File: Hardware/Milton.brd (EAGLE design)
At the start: 53 x 44.8 mm, 75 parts, among them J1 1981568-1, Q1 12MHz, U10 MAX31850K, U3 USD-SOCKETNEW, U4 MMA8452Q, U5 MIC5203-5.0YM5, U6 SI4464, U7 TPS61201, U8 BME280, U9 MMDT3904, X1 B4B-ZR

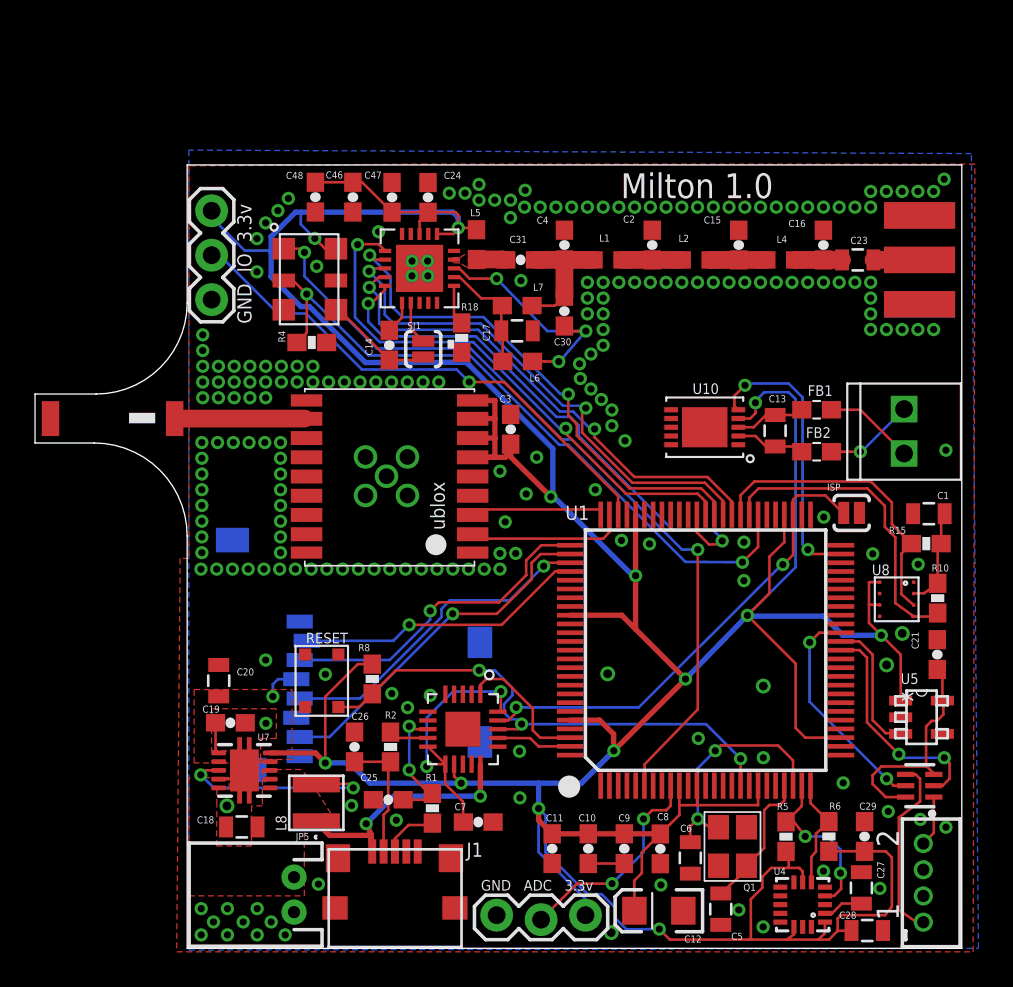
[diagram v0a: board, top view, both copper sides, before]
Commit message: Cleaning
Optimize traces, add more part numbers.
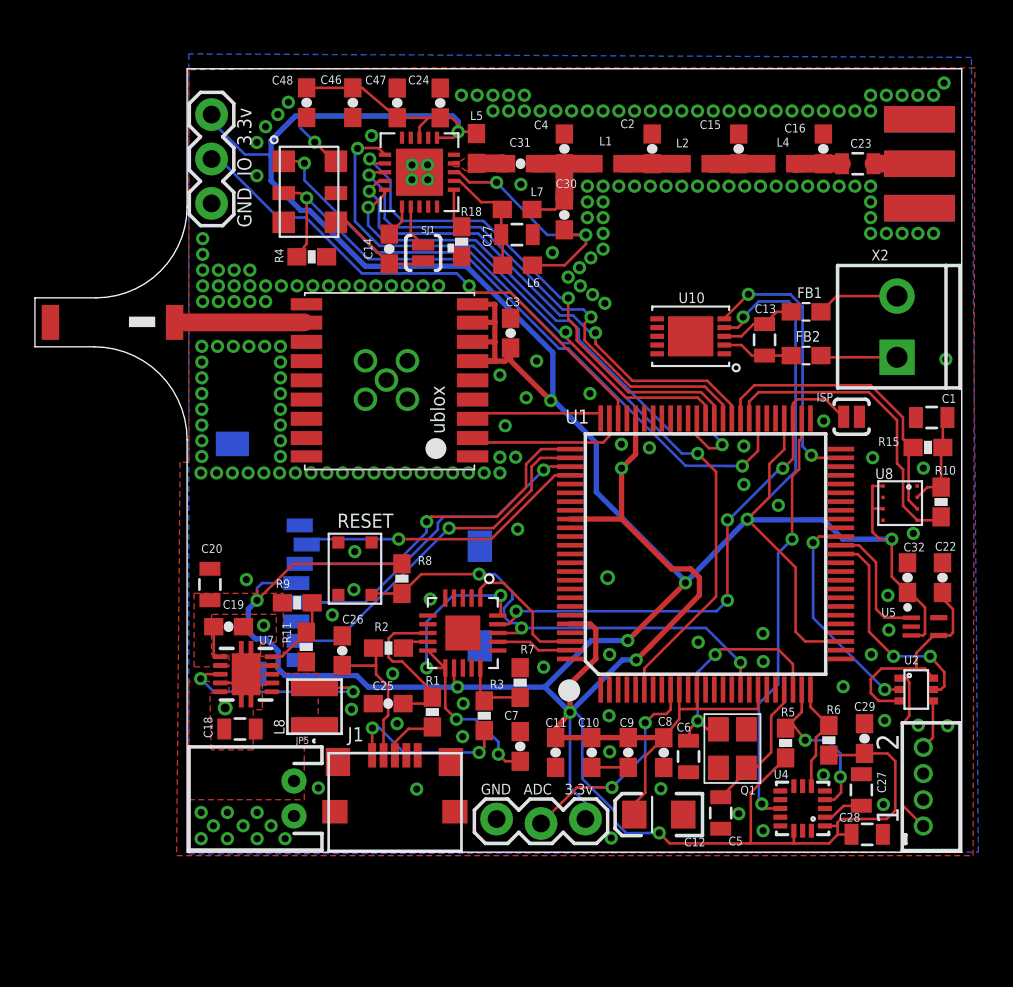
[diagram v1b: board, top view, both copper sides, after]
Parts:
- removed C21: 0.47uF, SparkFun-Capacitors:0603-CAP
- removed JP1: M022.54MM_SCREWTERM, SparkFun-Connectors:1X02_2.54_SCREWTERM
- removed U9: MMDT3904, SparkFun-DiscreteSemi:SOT363
- added C22, C32: 0.1uF, SparkFun-Capacitors:0603-CAP
- added R11: 180k, SparkFun-Resistors:0603-RES
- added R3: 4.7k, SparkFun-Resistors:0603-RES
- added R7: 10k, SparkFun-Resistors:0603-RES
- added R9: 1M, SparkFun-Resistors:0603-RES
- added U2: DDC113TU-7-F, wrea:SC70−6
- added X2: M023.5MM, SparkFun-Connectors:SCREWTERMINAL-3.5MM-2
- C7: value 100nf -> 0.1uF
- U5: value MIC5203-5.0YM5 -> TCR2EE50,LM; device wrea:SOT-23-5_M5 -> Xevelabs:SOT50P160X60-5N
- U7: value TPS61201 -> TPS61200
- moved RESET 6.68 mm to (9.60, 16.2)
- moved R8 5.98 mm to (12.3, 15.6)
- moved C6 5.80 mm to (28.7, 5.47)
- moved R2 5.66 mm to (11.5, 11.7), turned to 0 degrees
- moved FB1 5.63 mm to (35.4, 30.9)
- moved C18 5.60 mm to (3.02, 7.04)
- moved C27 5.60 mm to (38.6, 3.56)
- moved C29 5.60 mm to (38.7, 6.50)
- moved Q1 5.60 mm to (31.2, 5.92)
- moved C26 5.54 mm to (8.87, 11.5)
- moved FB2 5.53 mm to (35.4, 28.4)
- moved C20 5.52 mm to (1.30, 15.3)
- moved C9 5.50 mm to (25.2, 5.70)
- moved C10 5.50 mm to (23.1, 5.70)
- moved C11 5.50 mm to (21.1, 5.70)
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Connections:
- removed net N$16: U4.11
- new net N$1: R11.2, R9.1, U7.10
- new net N$10: J1.5, R3.2
- new net N$21: R3.1, R7.2, U$3.CBUS0
- net 3.3V: now also C32.1, R9.2, U5.3; no longer U4.7, U5.1, U7.10
- net 5V: now also C22.1, U2.3, U2.6, U5.4; no longer C21.2, U5.5, U9.3, U9.6
- net 5V_EN: now also U5.1; no longer U5.3
- net CAM1: now also U2.1; no longer U9.4
- net CAM2: now also U2.4; no longer U9.1
- net CAMERA1_EN: now also U2.2; no longer U9.5
- net CAMERA2_EN: now also U2.5; no longer U9.2
- net EINT1: now also U4.11
- net GND: now also C22.2, C32.2, R11.1, R7.1, U4.7; no longer C21.1
- net TM_RAW: now also X2.1; no longer JP1.P1
- net TP_RAW: now also X2.2; no longer JP1.P2
- net VIN: no longer J1.5, U$3.CBUS0
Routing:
- net 3.3V: track 275.4 -> 308.2 mm
- net EINT1: track 0.00 -> 24.3 mm, vias 0 -> 2
- net VIN: track 15.8 -> 0.00 mm, vias 2 -> 0
- net N$10: track 0.00 -> 9.62 mm, vias 0 -> 2
- net N$1: track 0.00 -> 4.54 mm
- net N$12: track 15.2 -> 19.5 mm, vias 2 -> 4
- net N$21: track 0.00 -> 4.15 mm
- net ISP_BOOT: track 27.6 -> 30.3 mm, vias 2 -> 4
- net RESET: track 30.5 -> 28.2 mm
- net N$4: track 7.58 -> 9.14 mm, vias 2 -> 0
- net N$9: track 7.43 -> 8.63 mm
- net CAM1: track 10.7 -> 9.53 mm
- net N$5: track 2.40 -> 1.55 mm
- net IC6_RTC2: track 14.1 -> 13.3 mm
- net TM_RAW: track 5.16 -> 4.39 mm, vias 1 -> 0
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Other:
- board text removed: "Milton 1.0"

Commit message: Update.
Shifted components to make room to break out another digital io
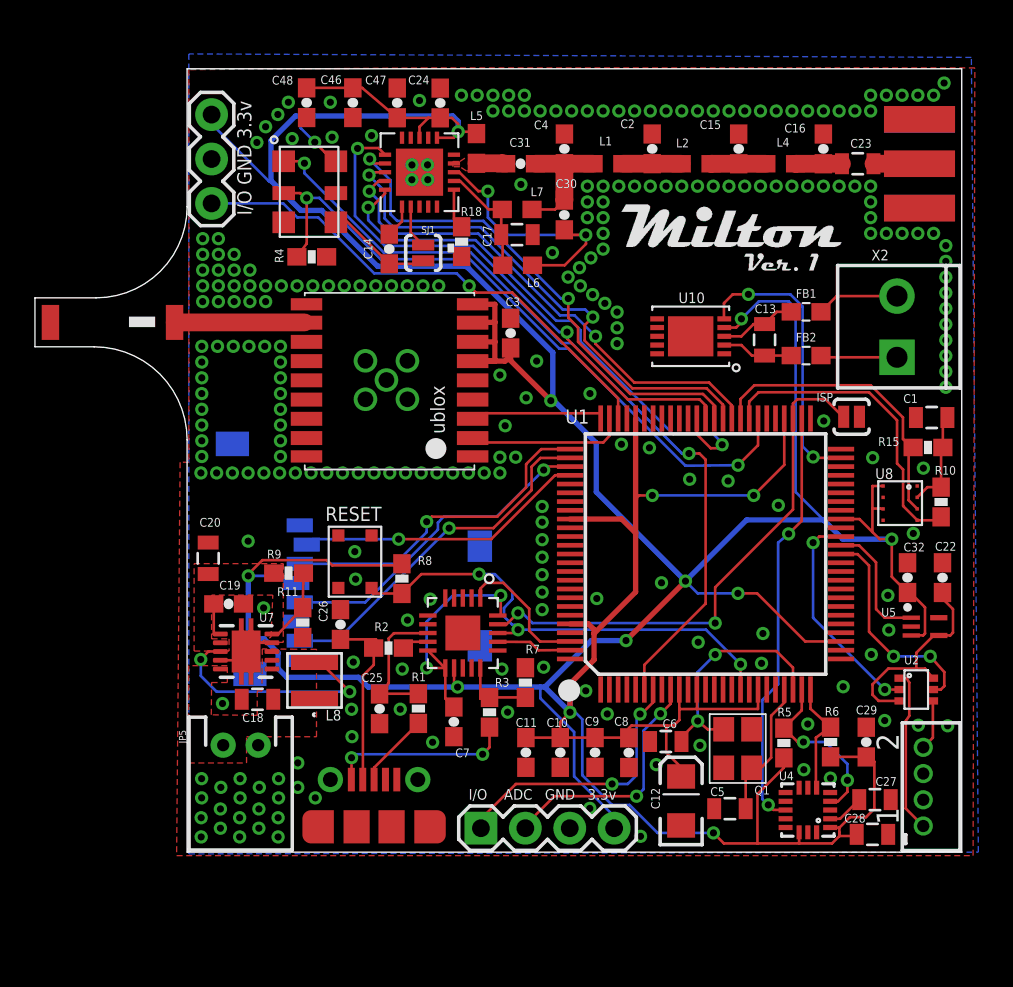
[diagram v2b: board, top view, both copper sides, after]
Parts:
- removed J1: 1981568-1, wrea:CONN_1981568-1
- removed JP2: (no value), SparkFun-Connectors:1X03_LOCK
- added JP1: (no value), SparkFun-Connectors:1X04
- added U$5: USB-CON-5PIN-105017-0001, GeekAmmo:USB-MICRO-MOLEX-105017-0001
- moved JP5 4.31 mm to (3.06, 6.12), turned to 180 degrees
- moved C7 4.05 mm to (15.3, 7.45), turned to 270 degrees
- moved C8 2.00 mm to (25.3, 5.69)
- moved C18 1.97 mm to (4.02, 8.74)
- moved C9 1.90 mm to (23.3, 5.70)
- moved C10 1.80 mm to (21.3, 5.70)
- moved R9 1.77 mm to (5.80, 16.0)
- moved C11 1.70 mm to (19.4, 5.70)
- moved C6 1.56 mm to (27.4, 6.33), turned to 180 degrees
- moved C20 1.50 mm to (1.20, 16.8)
- moved C26 1.50 mm to (8.77, 13.0)
- moved L8 1.50 mm to (7.28, 9.82)
- moved C12 1.50 mm to (28.2, 2.93), turned to 90 degrees
- moved R11 1.41 mm to (6.61, 13.1)
- moved C19 1.30 mm to (2.37, 14.2)
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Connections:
- removed net CUTDOWN: JP3.2, U1.73
- new net DIGITAL_1: JP3.1, U1.73
- new net DIGITAL_2: JP1.1, U1.7
- net 3.3V: now also JP1.4; no longer JP2.3
- net ADC_IN1: now also JP1.2; no longer JP2.2
- net GND: now also JP1.3, JP3.2, U$5.5; no longer J1.1, JP2.1, JP3.1
- net N$10: now also U$5.1; no longer J1.5
- net N$7: now also U$5.3; no longer J1.3
- net N$9: now also U$5.2; no longer J1.4
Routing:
- net CUTDOWN: track 30.2 -> 0.00 mm, vias 1 -> 0
- net DIGITAL_1: track 0.00 -> 29.0 mm, vias 0 -> 1
- net DIGITAL_2: track 0.00 -> 15.8 mm, vias 0 -> 2
- net N$12: track 19.5 -> 13.7 mm, vias 4 -> 2
- net N$9: track 8.63 -> 11.2 mm
- net ADC_IN1: track 12.3 -> 14.1 mm
- net GND: track 5.46 -> 3.95 mm, vias 216 -> 253
- net 3.3V: track 308.2 -> 306.7 mm
- net N$19: track 12.5 -> 13.9 mm
- net N$4: track 9.14 -> 7.95 mm
- net N$7: track 3.23 -> 4.26 mm
- net N$10: track 9.62 -> 10.5 mm
- net N$20: track 14.5 -> 15.3 mm
- net DAC: track 46.8 -> 46.1 mm
- net EXT_TEMP: track 15.8 -> 16.4 mm
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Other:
- board text added: "I/O ADC GND 3.3v"
- board text added: "I/O GND 3.3v"
- board text removed: "GND ADC 3.3v"
- board text removed: "GND IO 3.3v"

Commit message: Update
Continue cleaning up traces and adding part numbers
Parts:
- removed C46: 100pF, SparkFun-Capacitors:0603-CAP
- removed C47: 0.1uF, SparkFun-Capacitors:0603-CAP
- removed C48: 1uF, SparkFun-Capacitors:0603-CAP
- removed JP5: M02JST-PTH-2, SparkFun-Connectors:JST-2-PTH
- removed L8: SRN3015-2R2M, wrea:IND_BOURNS_SRN3015
- removed R15: 4.7k, SparkFun-Resistors:0603-RES
- removed U$5: USB-CON-5PIN-105017-0001, GeekAmmo:USB-MICRO-MOLEX-105017-0001
- added C21: 0.1uF, SparkFun-Capacitors:0805
- added C33: 36pF, SparkFun-Capacitors:0603-CAP
- added C34: 1000pF, SparkFun:0805
- added JP2: (no value), SparkFun-Connectors:1X03
- added L3: 220nH, SparkFun-Passives:0603
- added R12: 1k, SparkFun-Resistors:0603-RES
- added U9: BME280, wrea:BME280
- C1: value 0.1uF -> 47pF; device SparkFun-Capacitors:0805 -> SparkFun-Capacitors:0603-CAP
- C10: value 0.1uF -> 10uF; device SparkFun-Capacitors:0603-CAP -> SparkFun-Capacitors:EIA3216
- C11: device SparkFun-Capacitors:0603-CAP -> SparkFun:0603-CAP
- C12: device SparkFun-Capacitors:EIA3216 -> SparkFun-Capacitors:0805
- C13: device SparkFun-Capacitors:0805 -> SparkFun-Capacitors:0603-CAP
- C14: value 100pF -> 10uF; device SparkFun-Capacitors:0603-CAP -> SparkFun-Capacitors:0805
- C15: value 56pF -> 0.1uF
- C16: value 36pF -> 0.1uF
- C17: value 22pF -> 0.1uF; device SparkFun:0805 -> SparkFun-Capacitors:0805
- C18: value 10uF -> 4.7uF; device SparkFun-Capacitors:0805 -> SparkFun-Capacitors:0603-CAP
- C19: device SparkFun-Capacitors:0603-CAP -> SparkFun-Capacitors:0805
- C2: value 56pF -> 47pF
- C20: value 10uF -> 0.1uF
- C22: value 0.1uF -> 100pF
- C23: value 1000pF -> 1uF; device SparkFun:0805 -> SparkFun-Capacitors:0603-CAP
- C24: value 1000pF -> 0.1uF
- C25: value 47pF -> 100pF
- C26: value 47pF -> 22pF; device SparkFun-Capacitors:0603-CAP -> SparkFun:0805
- C27, C28: value 0.1uF -> 1000pF; device SparkFun-Capacitors:0805 -> SparkFun-Capacitors:0603-CAP
- C29: value 4.7uF -> 12pF
- C3: device SparkFun:0603-CAP -> SparkFun-Capacitors:0603-CAP
- C30: value 12pF -> 36pF
- C31: value 1000pF -> 56pF
- C32: value 0.1uF -> 56pF
- C4: value 36pF -> 18pF; device SparkFun-Capacitors:0603-CAP -> SparkFun-Capacitors:0805
- C6: value 18pF -> 0.1uF; device SparkFun-Capacitors:0805 -> SparkFun-Capacitors:0603-CAP
- FB1, FB2: value (none) -> FB; device LoganSmith-Inductors:0603-RES -> SparkFun-Passives:0603
- JP1: value (none) -> M02JST-PTH-2; device SparkFun-Connectors:1X04 -> SparkFun-Connectors:JST-2-PTH
- JP3: device SparkFun-Connectors:1X03 -> SparkFun-Connectors:1X04
- L1: value 68nH -> SRN3015-2R2M; device SparkFun-Passives:0603 -> wrea:IND_BOURNS_SRN3015
- L2: value 72nH -> 470nH
- L4: value 68nH -> 150nH
- L5: value 470nH -> 68nH
- L6: value 220nH -> 72nH
- L7: value 150nH -> 68nH
- R1: value 27 -> 4.7k
- R11: value 180k -> 4.7k
- R2: value 27 -> 10k
- R3: value 4.7k -> 27
- R4: value 1k -> 27
- R5: value 4.7k -> 10K
- R6: value 4.7k -> 1M
- R7: value 10k -> 180k
- R8: value 10K -> 4.7k
- R9: value 1M -> 4.7k
- U$1: value 1575AT43A40 -> USB-MICRO_105017-0001; device ava:JTI_ANTENNA-1575AT43A40 -> wrea:USB-MICRO-MOLEX-105017-0001
- U$2: value UBLOX_MAX -> 1575AT43A40; device ava:UBLOX_MAX -> ava:JTI_ANTENNA-1575AT43A40
- U$3: value FT231XQ-R -> UBLOX_MAX; device ftdi_ft231xq-r:FTDI_FT231XQ-R_PACKAGE -> ava:UBLOX_MAX
- U1: value (none) -> FT231X; device microbuilder:LQFP100 -> wrea:FT231XQ-R
- U10: value MAX31850K -> SI4464; device LoganSmith-Analog_IC:10-TDFN-EP -> ava:QFN20+GNDPAD
- U2: value DDC113TU-7-F -> (none); device wrea:SC70−6 -> microbuilder:LQFP100
- U4: value MMA8452Q -> DDC113TU-7-F; device SparkFun-Sensors:QFN-16_0.5MM -> wrea:SC70−6
- U5: value TCR2EE50,LM -> TPS61200; device Xevelabs:SOT50P160X60-5N -> texas:S-PDSO-N10
- U6: value SI4464 -> TCR2EE50,LM; device ava:QFN20+GNDPAD -> Xevelabs:SOT50P160X60-5N
- U7: value TPS61200 -> MMA8452Q; device texas:S-PDSO-N10 -> SparkFun-Sensors:QFN-16_0.5MM
- U8: value BME280 -> MAX31850K; device wrea:BME280 -> LoganSmith-Analog_IC:10-TDFN-EP
- moved C27 47.0 mm to (14.5, 42.8), turned to 270 degrees
- moved C28 43.3 mm to (19.1, 39.4), turned to 180 degrees
- moved C17 39.9 mm to (39.2, 1.02), turned to 0 degrees
- moved JP3 38.9 mm to (16.8, 1.37), turned to 0 degrees
- moved C4 38.9 mm to (31.0, 2.49), turned to 180 degrees
- moved U6 38.9 mm to (42.2, 12.9), turned to 0 degrees
- moved U5 38.9 mm to (3.37, 11.5), turned to 270 degrees
- moved C19 38.6 mm to (39.3, 3.00)
- moved R11 37.2 mm to (43.1, 20.0)
- moved C22 36.8 mm to (11.6, 34.5), turned to 270 degrees
- moved C1 35.8 mm to (8.77, 13.0), turned to 270 degrees
- moved C2 35.6 mm to (11.0, 8.20), turned to 270 degrees
- moved C18 34.9 mm to (38.8, 6.29), turned to 90 degrees
- moved C29 34.7 mm to (21.6, 36.4), turned to 270 degrees
- moved C25 34.7 mm to (9.47, 42.9)
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- renumbered J$3 to J$1, R18 to R13
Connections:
- removed net RSTOUT: U1.14
- removed net RTCK: U1.100
- removed net RXD1: U$2.2_TXD1, U1.74
- removed net TCK: U1.5
- removed net TDI: U1.2
- removed net TDO: U1.1
- removed net TMS: U1.3
- removed net TXD1: U$2.3_RXD1, U1.75
- net 10_GND: now also U$3.10_GND; no longer U$2.10_GND
- net 12_GND: now also U$3.12_GND; no longer U$2.12_GND
- net 3.3V: now also C10.A, C11.1, C14.1, C16.1, C17.1, C18.1, C21.1, C23.1, C24.1, C25.1, C27.2, C6.2, C7.2, JP2.3, JP3.4, L2.1, R11.2, U$3.6_V_BCKP, U$3.7_VCC_IO, U$3.8_VCC, U$3.9_V_RESET, U1.VCC, U10.6, U10.8, U2.10, U2.12, U2.19, U2.28, U2.42, U2.54, U2.71, U2.84, U2.96, U5.2, U6.3, U7.1, U7.14, U8.4, U9.2, U9.6, U9.8; no longer C1.1, C10.2, C11.2, C12.A, C20.1, C24.2, C28.1, C29.1, C3.1, C32.1, C46.1, C47.1, C48.1, JP1.4, JP3.3, L5.1, R15.2, U$2.6_V_BCKP, U$2.7_VCC_IO, U$2.8_VCC, U$2.9_V_RESET, U$3.VCC, U1.10, U1.12, U1.19, U1.28, U1.42, U1.54, U1.71, U1.84, U1.96, U10.4, U4.1, U4.14, U5.3, U6.6, U6.8, U7.2, U8.2, U8.6, U8.8
- net 5V: now also C15.1, U4.3, U4.6, U6.4; no longer C22.1, U2.3, U2.6, U5.4
- net 5V_EN: now also U2.39, U6.1; no longer U1.39, U5.1
- net ADC_IN1: now also JP3.2, U2.9; no longer JP1.2, U1.9
- net ADC_IN2: now also U2.8; no longer U1.8
- net CAM1: now also U4.1; no longer U2.1
- net CAM2: now also U4.4; no longer U2.4
- net CAMERA1_EN: now also U2.40, U4.2; no longer U1.40, U2.2
- net CAMERA2_EN: now also U2.38, U4.5; no longer U1.38, U2.5
- net DAC: now also U2.6; no longer U1.6
- net DIGITAL_1: now also JP2.1, U2.73; no longer JP3.1, U1.73
- net DIGITAL_2: now also JP3.1, U2.7; no longer JP1.1, U1.7
- net EINT1: now also U2.52, U7.11; no longer U1.52, U4.11
- net EXT_TEMP: now also U2.49, U8.5; no longer U1.49, U10.5
- net GND: now also C1.1, C10.C, C11.2, C12.2, C13.2, C14.2, C17.2, C21.2, C23.2, C24.2, C27.1, C30.2, C31.2, C33.2, C6.1, C7.1, JP1.1, JP2.2, JP3.3, R12.1, R2.1, U$1.5, U$3.1_GND, U$3.4_TIMEPULSE, U1.GND_PIN13, U1.GND_PIN21, U1.GND_PIN3, U10.18, U10.21, U2.11, U2.15, U2.31, U2.41, U2.55, U2.72, U2.83, U2.97, U5.4, U5.9, U5.PP, U5.PP@1, U5.PP@2, U6.2, U7.10, U7.12, U7.5, U7.7, U8.6, U8.8, U8.9, U8.PAD, U9.1, U9.5, U9.7; no longer C1.2, C10.1, C11.1, C12.C, C17.1, C20.2, C22.2, C24.1, C27.2, C28.2, C29.2, C46.2, C47.2, C48.2, C6.2, C7.2, JP1.3, JP3.2, JP5.1, R11.1, R4.1, U$2.1_GND, U$2.4_TIMEPULSE, U$3.GND_PIN13, U$3.GND_PIN21, U$3.GND_PIN3, U$5.5, U1.11, U1.15, U1.31, U1.41, U1.55, U1.72, U1.83, U1.97, U10.1, U10.6, U10.7, U10.8, U10.9, U10.PAD, U4.10, U4.12, U4.5, U4.7, U5.2, U6.18, U6.21, U7.4, U7.9, U7.PP, U7.PP@1, U7.PP@2, U8.5
- net IC6_RTC1: now also C4.1, U2.22; no longer C5.1, U1.22
- net IC6_RTC2: now also C5.1, U2.23; no longer C6.1, U1.23
- net ISP_BOOT: now also U1.RTS#, U2.53; no longer U$3.RTS#, U1.53
- net N$1: now also R6.1, R7.2, U5.10; no longer R11.2, R9.1, U7.10
- net N$10: now also R1.2, U$1.1; no longer R3.2, U$5.1
- net N$11: now also C32.1, L6.1, L7.2; no longer C15.1, L2.1, L4.2
- net N$12: now also C3.1, U1.3V3OUT, U1.RESET#, U1.VCCIO; no longer C7.1, U$3.3V3OUT, U$3.RESET#, U$3.VCCIO
- net N$18: now also C28.2, L2.2, U10.4; no longer C31.2, L5.2, U6.4
- net N$19: now also L1.1, U5.3; no longer L8.1, U7.3
- net N$2: now also C19.1, U7.2; no longer C27.1, U4.2
- net N$20: now also C29.2, L3.2, U10.3; no longer C30.2, L6.2, U6.3
- net N$21: now also R1.1, R2.2, U1.CBUS0; no longer R3.1, R7.2, U$3.CBUS0
- net N$28: now also C22.2; no longer C14.2
- net N$29: now also C26.2, L3.1, L4.2, U10.2; no longer C17.2, L6.1, L7.2, U6.2
- net N$30: now also C33.1, C34.2, L7.1; no longer C16.1, C23.2, L4.1
- net N$33: now also C34.1; no longer C23.1
- net N$36: now also C28.1, C29.1, L4.1, L5.2; no longer C31.1, C4.1, L1.2, L7.1
- net N$37: now also C31.1, L5.1, L6.2; no longer C2.1, L1.1, L2.2
- net N$38: now also U10.17; no longer U6.17
- net N$4: now also C2.1, R3.2, U1.USBDP; no longer C25.1, R1.2, U$3.USBDP
- net N$5: now also R4.2, U1.USBDM; no longer R2.2, U$3.USBDM
- net N$6: now also C22.1, U10.16; no longer C14.1, U6.16
- net N$7: now also R3.1, U$1.3; no longer R1.1, U$5.3
- net N$8: now also U$2.FEED, U$3.11_RF_IN; no longer U$1.FEED, U$2.11_RF_IN
- net N$9: now also C1.2, R4.1, U$1.2; no longer C26.2, R2.1, U$5.2
- net RADIO_EN: now also U10.1; no longer U6.1
- net RADIO_SEL: now also U10.15, U2.64; no longer U1.64, U6.15
- net RESET: now also R5.1, U1.DTR#, U2.17; no longer R8.1, U$3.DTR#, U1.17
- net RF_MISO: now also U10.13, U2.61; no longer U1.61, U6.13
- net RF_MOSI: now also U10.14, U2.60; no longer U1.60, U6.14
- net RF_NIRQ: now also U10.11, U2.63; no longer U1.63, U6.11
- net RF_SCK: now also U10.12, U2.62; no longer U1.62, U6.12
- net RXD0: now also U$3.2_TXD1, U1.TXD, U2.99; no longer U$3.TXD, U1.99
- net SCL0: now also R8.1, U2.24, U7.4; no longer R5.1, U1.24, U4.4
- net SCL1: now also R11.1, U2.58, U9.4; no longer R10.1, U1.58, U8.4
- net SDA0: now also R9.1, U2.25, U7.6; no longer R6.1, U1.25, U4.6
- net SDA1: now also R10.1, U2.59, U9.3; no longer R15.1, U1.59, U8.3
- net SD_CS: now also U2.79; no longer U1.79
- net SD_MISO: now also U2.77; no longer U1.77
- net SD_MOSI: now also U2.76; no longer U1.76
- net SD_SCK: now also U2.78; no longer U1.78
- net TM_FILT: now also C20.2, FB2.1, U8.2; no longer C13.2, FB2.P$2, U10.2
- net TM_RAW: now also FB2.2; no longer FB2.P$1
- net TP_FILT: now also C20.1, FB1.1, U8.3; no longer C13.1, FB1.P$2, U10.3
- net TP_RAW: now also FB1.2; no longer FB1.P$1
- net TRST: now also U2.4; no longer U1.4
- net TXD0: now also U$3.3_RXD1, U1.RXD, U2.98; no longer U$3.RXD, U1.98
- net VAUX: now also C13.1, U5.1; no longer C19.1, U7.1
- net VIN: now also C12.1, JP1.2, L1.2, U5.5, U5.6, U5.7, U5.8; no longer C18.1, JP5.2, L8.2, U7.5, U7.6, U7.7, U7.8
- net XTAL_EN: now also R12.2, U2.57; no longer R4.2, U1.57
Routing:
- net TXD0: track 7.93 -> 27.3 mm, vias 0 -> 2
- net RXD0: track 4.33 -> 22.9 mm, vias 0 -> 2
- net 3.3V: track 306.7 -> 292.8 mm, vias 14 -> 12
- net RXD1: track 9.10 -> 0.00 mm
- net TXD1: track 7.70 -> 0.00 mm
- net ISP_BOOT: track 30.8 -> 33.0 mm
- net TP_FILT: track 4.41 -> 6.11 mm
- net TM_FILT: track 4.08 -> 5.78 mm
- net TM_RAW: track 4.39 -> 6.05 mm
- net TP_RAW: track 4.72 -> 6.20 mm
- net DAC: track 46.1 -> 45.0 mm
- net N$7: track 4.26 -> 5.13 mm
- net RESET: track 28.2 -> 29.0 mm
- net N$19: track 13.9 -> 14.6 mm
- net GND: vias 253 -> 316
